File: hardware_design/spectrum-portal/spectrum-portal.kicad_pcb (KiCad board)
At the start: 4 copper layers, 23 x 97.8 mm, 32 parts, among them J1 PJ398SM, J2 PJ398SM, J4 PJ398SM, J5 PJ398SM, J7 SBH11-PBPC-D05-ST-BK, U1 TL072IDR

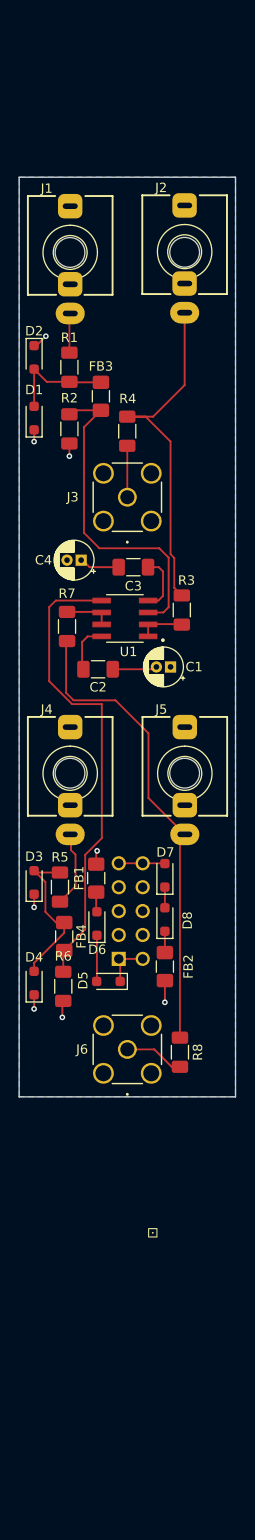
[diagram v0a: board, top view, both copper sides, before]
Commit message: Redesigned as passive module in 3HP
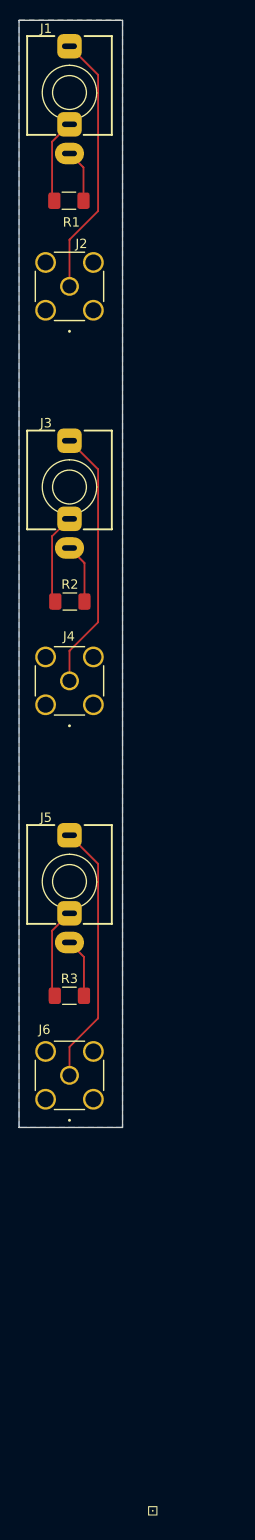
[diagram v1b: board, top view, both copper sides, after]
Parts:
- removed C1, C4: 10µF 25V, Capacitor_THT:CP_Radial_D4.0mm_P1.50mm
- removed C2, C3: 0.1µF 25V, Capacitor_SMD:C_1206_3216Metric_Pad1.33x1.80mm_HandSolder
- removed D1, D2, D3, D4: PJGBLC15C_R1_00001, Diode_SMD:D_SOD-323_HandSoldering
- removed D5, D7: NSR0530HT1G, Diode_SMD:D_SOD-323_HandSoldering
- removed D6, D8: D12V0H1U2WS-7, Diode_SMD:D_SOD-323_HandSoldering
- removed FB1, FB2, FB3, FB4: 2512066017Y1, Inductor_SMD:L_1206_3216Metric_Pad1.42x1.75mm_HandSolder
- removed the J2 at (124.0, 65.9)
- removed J7: SBH11-PBPC-D05-ST-BK, EurorackPowerConnector:SULLINS_SBH11-PBPC-D05-ST-BK
- removed R4, R8: 47Ω, Resistor_SMD:R_1206_3216Metric_Pad1.30x1.75mm_HandSolder
- removed R5: 1KΩ, Resistor_SMD:R_1206_3216Metric_Pad1.30x1.75mm_HandSolder
- removed R6: 100KΩ, Resistor_SMD:R_1206_3216Metric_Pad1.30x1.75mm_HandSolder
- removed R7: 100Ω, Resistor_SMD:R_1206_3216Metric_Pad1.30x1.75mm_HandSolder
- removed U1: TL072IDR, TL072:SOIC127P599X175-8N
- added J3: PJ398SM, Thonk:Jack_3.5mm_QingPu_WQP-PJ398SM_Vertical, F.Cu at (111.8, 90.9)
- J4: value PJ398SM -> ~; footprint Thonk:Jack_3.5mm_QingPu_WQP-PJ398SM_Vertical -> SMA:CONN_132291_AMP
- R1: value 1KΩ -> 100K
- R2: value 100KΩ -> 100K
- R3: value 100Ω -> 100K
- moved R3 42.7 mm to (111.8, 145.0), turned to 0 degrees
- moved J2 23.2 mm to (111.8, 69.6)
- moved R2 18.4 mm to (111.8, 103.1), turned to 0 degrees
- moved R1 17.7 mm to (111.7, 60.5), turned to 0 degrees
- moved J1 17.0 mm to (111.8, 49.0)
- moved J5 16.8 mm to (111.8, 132.9)
- moved J4 9.83 mm to (111.8, 111.5), turned to -90 degrees
- moved J6 6.74 mm to (111.8, 153.5)
- renumbered J3 to J2
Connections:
- J1 pad S: Net-(J1-PadS) -> GND
- J1 pad T: GND -> Net-(J2-In)
- J1 pad TN: (no net) -> Net-(J1-PadTN)
- J2 pad 1: Net-(J3-In) -> Net-(J2-In)
- J5 pad S: Net-(J5-PadS) -> GND
- J5 pad T: GND -> Net-(J6-In)
- J5 pad TN: (no net) -> Net-(J5-PadTN)
- R1 pad 1: Net-(J1-PadS) -> Net-(J1-PadTN)
- R1 pad 2: Net-(D1-A) -> GND
- R3 pad 1: Net-(U1A--) -> Net-(J5-PadTN)
- R3 pad 2: Net-(J2-PadS) -> GND
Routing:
- net Net-(J5-PadS): track 51.0 -> 0.00 mm
- net Net-(U1B-+): track 50.9 -> 0.00 mm
- net Net-(J2-PadS): track 36.9 -> 0.00 mm
- net Net-(J2-In): track 0.00 -> 28.0 mm
- net Net-(J4-In): track 0.00 -> 28.0 mm
- net Net-(J3-PadTN): track 34.7 -> 9.70 mm
- net Net-(J6-In): track 6.36 -> 28.0 mm
- net Net-(D3-A): track 16.7 -> 0.00 mm
- net GND: track 3.00 -> 18.3 mm, vias 2 -> 0
- net Net-(D1-A): track 11.7 -> 0.00 mm
- net Net-(J5-PadTN): track 0.00 -> 9.65 mm
- net Net-(J1-PadTN): track 0.00 -> 8.99 mm
- net Net-(J4-PadS): track 8.07 -> 0.00 mm
- net Net-(U1C-V-): track 6.16 -> 0.00 mm
- net Net-(J3-In): track 5.46 -> 0.00 mm
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- added copper zone on B.Cu, net GND
- removed copper zone on In2.Cu, net +12V
- removed copper zone on B.Cu, net -12V
- removed copper zone on In1.Cu, net GND
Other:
- board size 23 x 97.8 mm -> 11 x 117.7 mm
- copper layers 4 -> 2
